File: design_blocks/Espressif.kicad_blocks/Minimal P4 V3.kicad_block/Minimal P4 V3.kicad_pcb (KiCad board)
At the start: 4 copper layers, 43 parts, among them U1 TLV62569DBV, U3 W25Q128JVS, Y1 40MHz(+-10 ppm) C501798

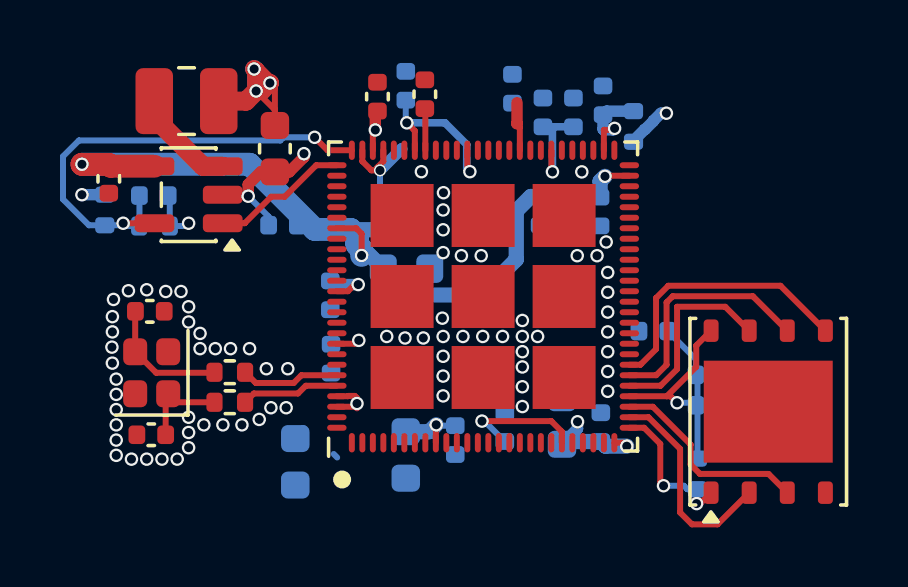
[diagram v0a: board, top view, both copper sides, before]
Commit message: Add reset RC to pcb layout
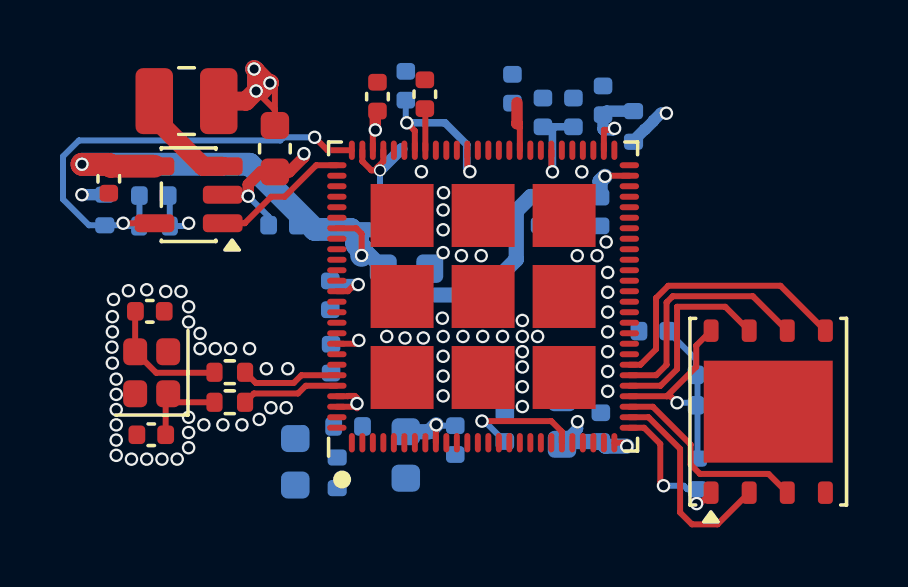
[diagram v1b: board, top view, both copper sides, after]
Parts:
- added C33: 0.1uF, Capacitor_SMD:C_0402_1005Metric, B.Cu at (171.7, 89.0)
- added R200: 10k, Resistor_SMD:R_0402_1005Metric, B.Cu at (171.3, 90.5)
